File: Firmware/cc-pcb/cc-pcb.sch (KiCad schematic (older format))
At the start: 17 parts, among them CON1 BARREL_JACK, IC1 ATMEGA328P-A, P1 CONN_6, P2 CONN_6, P3 CONN_10, P4 CONN_6, P5 CONN_6, SW1 SRS

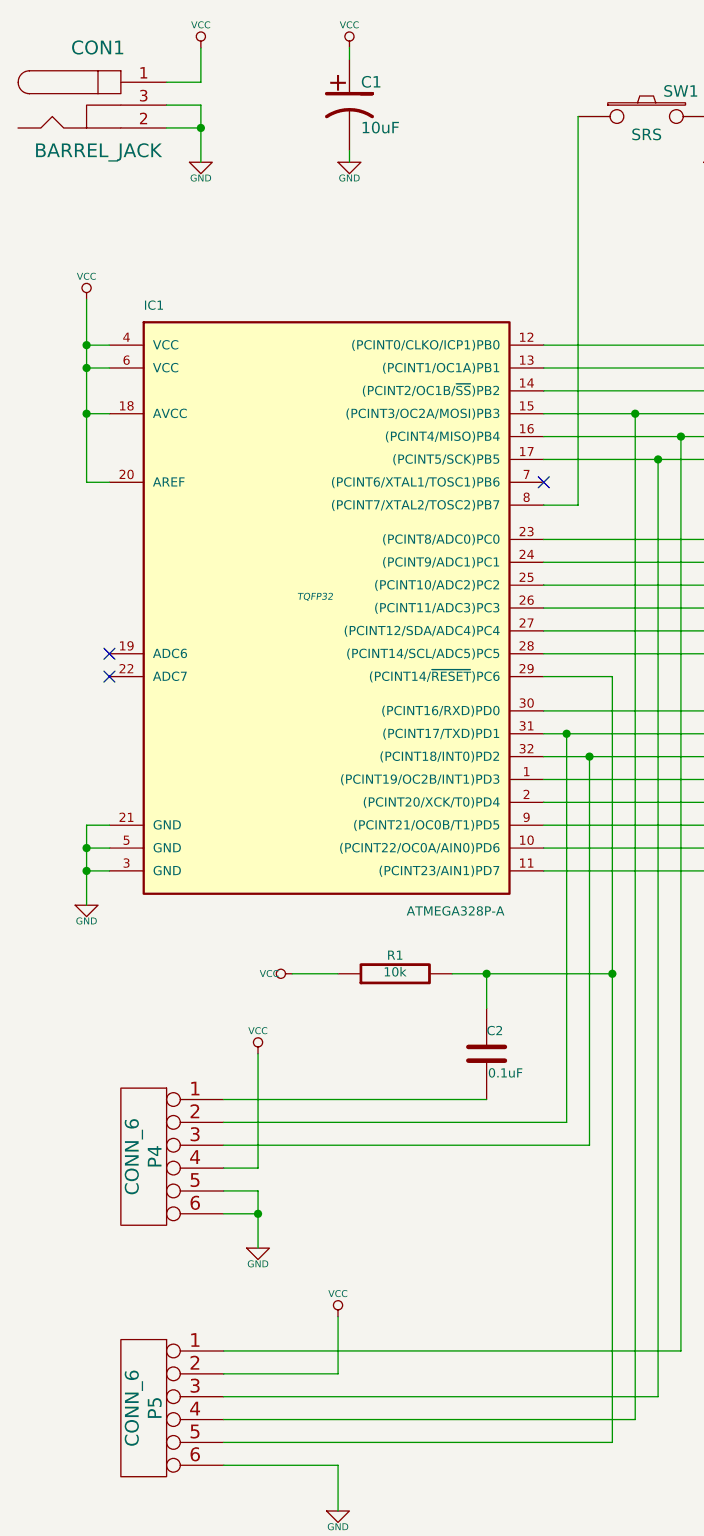
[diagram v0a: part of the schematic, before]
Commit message: Finishing schematics for PCB
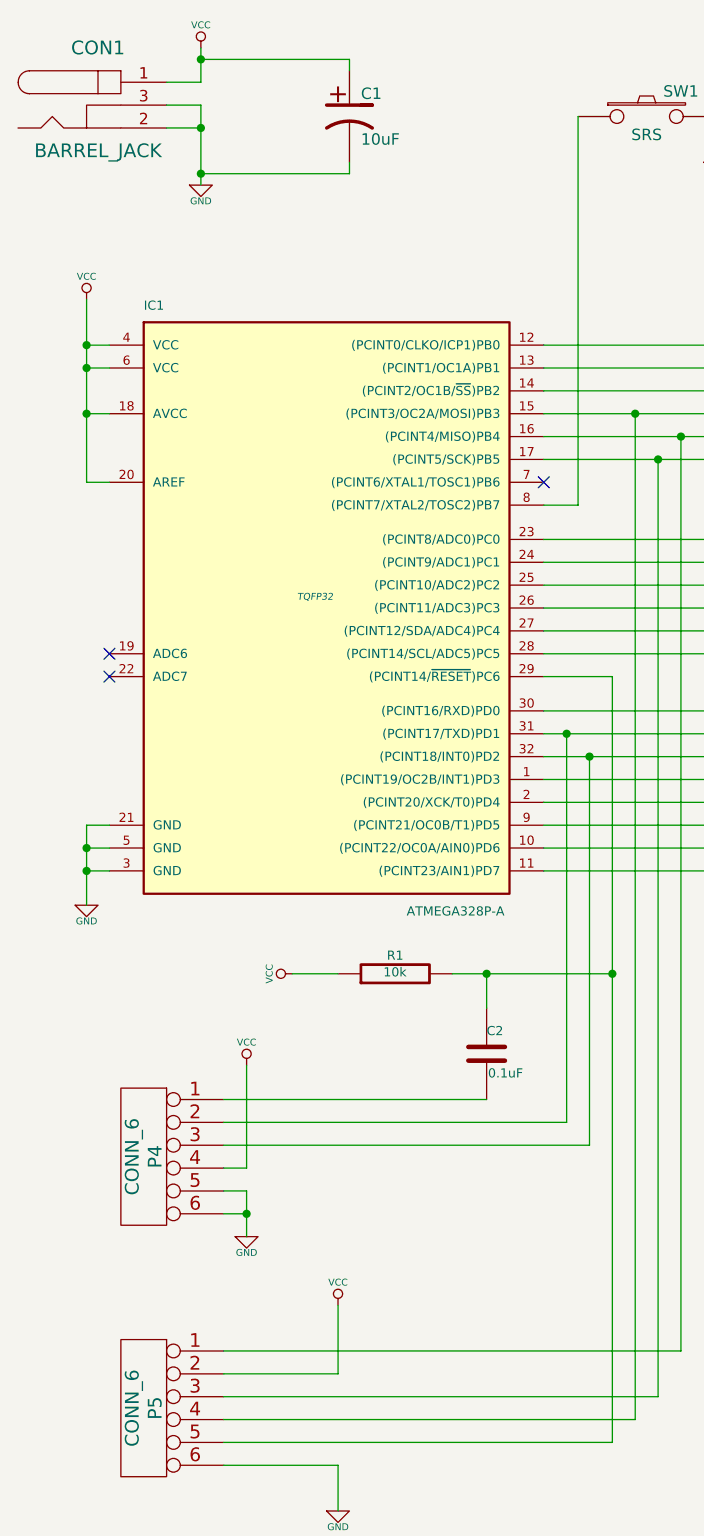
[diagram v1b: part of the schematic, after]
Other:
- moved on the sheet: C1

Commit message: Working on PCB
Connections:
- net VCC: no longer IC1.20 (AREF)
- no-connect marks 3 -> 4
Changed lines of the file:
@@
 Sheet 1 1
 Title "cc-schema.sch"
-Date "1 sep 2014"
+Date "2 sep 2014"
 Rev ""
 Comp ""
@@
 Wire Wire Line
 	2300 4100 2200 4100
-Connection ~ 2200 2100
-Wire Wire Line
-	2200 2100 2300 2100
-Connection ~ 2200 2000
-Wire Wire Line
-	2300 2000 2200 2000
 Wire Wire Line
 	5800 5300 6100 5300
@@
 Wire Wire Line
 	4800 6400 2800 6400
-Connection ~ 2200 2300
-Wire Wire Line
-	2200 2600 2300 2600
 Connection ~ 3950 4750
 Wire Wire Line
@@
 	2200 2300 2300 2300
 Wire Wire Line
-	2200 1800 2200 2600
-Wire Wire Line
-	2700 850  2700 700
-Wire Wire Line
-	2550 850  2700 850
+	2700 700  2700 850
+Wire Wire Line
+	2700 850  2550 850
 Connection ~ 2700 1050
 Wire Wire Line
@@
 	3350 1250 2700 1250
 Connection ~ 2700 1250
+$Comp
+L PWR_FLAG #FLG013
+U 1 1 5405B6E7
+P 2700 700
+F 0 "#FLG013" H 2700 795 30  0001 C CNN
+F 1 "PWR_FLAG" H 2700 880 30  0000 C CNN
+F 2 "" H 2700 700 60  0000 C CNN
+F 3 "" H 2700 700 60  0000 C CNN
+	1    2700 700
+	0    -1   -1   0
+$EndComp
+$Comp
+L PWR_FLAG #FLG014
+U 1 1 5405B6F6
+P 2700 1300
+F 0 "#FLG014" H 2700 1395 30  0001 C CNN
+F 1 "PWR_FLAG" H 2700 1480 30  0000 C CNN
+F 2 "" H 2700 1300 60  0000 C CNN
+F 3 "" H 2700 1300 60  0000 C CNN
+	1    2700 1300
+	0    -1   -1   0
+$EndComp
+NoConn ~ 2300 2600
+Wire Wire Line
+	2200 2300 2200 1800
+Wire Wire Line
+	2300 2100 2200 2100
+Connection ~ 2200 2100
+Wire Wire Line
+	2300 2000 2200 2000
+Connection ~ 2200 2000
 $EndSCHEMATC

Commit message: Finalyzing component list, fixing errors
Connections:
- net at IC1.30 ((PCINT16/RXD)PD0), P3.1 (P1): now also P4.3
- net at IC1.32 ((PCINT18/INT0)PD2), P3.3 (P3): no longer P4.3
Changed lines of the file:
@@
 Sheet 1 1
 Title "cc-schema.sch"
-Date "2 sep 2014"
+Date "4 sep 2014"
 Rev ""
 Comp ""
@@
 	2300 4200 2200 4200
 Wire Wire Line
-	2200 4100 2200 4450
+	2200 4100 2200 4200
+Wire Wire Line
+	2200 4200 2200 4300
+Wire Wire Line
+	2200 4300 2200 4450
 Wire Wire Line
 	2300 4100 2200 4100
@@
 Wire Wire Line
 	4200 3900 5500 3900
-Connection ~ 4400 3800
 Wire Wire Line
 	5600 3800 5600 4600
@@
 	5800 3600 5800 4400
 Wire Wire Line
-	4200 3600 5800 3600
+	4200 3600 4400 3600
+Wire Wire Line
+	4400 3600 5800 3600
 Connection ~ 4600 2300
 Connection ~ 4700 2500
@@
 	4500 3450 4200 3450
 Wire Wire Line
-	4500 3450 4500 6800
-Wire Wire Line
-	3800 4750 4500 4750
+	4500 3450 4500 4750
+Wire Wire Line
+	4500 4750 4500 6800
+Wire Wire Line
+	3800 4750 3950 4750
+Wire Wire Line
+	3950 4750 4500 4750
 Wire Wire Line
 	3100 4750 3300 4750
@@
 	2200 2300 2300 2300
 Wire Wire Line
-	2700 700  2700 850
+	2700 700  2700 750
+Wire Wire Line
+	2700 750  2700 850
 Wire Wire Line
 	2700 850  2550 850
@@
 	2550 1050 2700 1050
 Wire Wire Line
-	2700 950  2700 1300
+	2700 950  2700 1050
+Wire Wire Line
+	2700 1050 2700 1250
+Wire Wire Line
+	2700 1250 2700 1300
 Wire Wire Line
 	2550 950  2700 950
@@
 	4200 3800 5600 3800
 Wire Wire Line
-	4400 3800 4400 5500
+	4400 3600 4400 5500
 Wire Wire Line
 	4400 5500 2800 5500
 Wire Wire Line
-	4200 3700 5700 3700
+	4200 3700 4300 3700
+Wire Wire Line
+	4300 3700 5700 3700
 Wire Wire Line
 	4300 3700 4300 5400
@@
 	4350 2700 4350 1000
 Wire Wire Line
-	4200 2500 7600 2500
-Wire Wire Line
-	4200 2400 7200 2400
-Wire Wire Line
-	4200 2300 6800 2300
+	4200 2500 4700 2500
+Wire Wire Line
+	4700 2500 7600 2500
+Wire Wire Line
+	4200 2400 4800 2400
+Wire Wire Line
+	4800 2400 7200 2400
+Wire Wire Line
+	4200 2300 4600 2300
+Wire Wire Line
+	4600 2300 6800 2300
 Wire Wire Line
 	4200 2200 6400 2200
@@
 	2800 5700 2900 5700
 Wire Wire Line
-	2900 5700 2900 5900
+	2900 5700 2900 5800
+Wire Wire Line
+	2900 5800 2900 5900
 Wire Wire Line
 	2800 5800 2900 5800
@@
 NoConn ~ 2300 2600
 Wire Wire Line
-	2200 2300 2200 1800
+	2200 2300 2200 2100
+Wire Wire Line
+	2200 2100 2200 2000
+Wire Wire Line
+	2200 2000 2200 1800
 Wire Wire Line
 	2300 2100 2200 2100
@@
 	2300 2000 2200 2000
 Connection ~ 2200 2000
+Connection ~ 4400 3600
 $EndSCHEMATC

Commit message: Finalyzing component list, fixing errors
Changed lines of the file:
@@
 	2300 4200 2200 4200
 Wire Wire Line
-	2200 4100 2200 4200
-Wire Wire Line
-	2200 4200 2200 4300
-Wire Wire Line
-	2200 4300 2200 4450
+	2200 4100 2200 4450
 Wire Wire Line
 	2300 4100 2200 4100
@@
 	5800 3600 5800 4400
 Wire Wire Line
-	4200 3600 4400 3600
-Wire Wire Line
-	4400 3600 5800 3600
+	4200 3600 5800 3600
 Connection ~ 4600 2300
 Connection ~ 4700 2500
@@
 	4500 3450 4200 3450
 Wire Wire Line
-	4500 3450 4500 4750
-Wire Wire Line
-	4500 4750 4500 6800
-Wire Wire Line
-	3800 4750 3950 4750
-Wire Wire Line
-	3950 4750 4500 4750
+	4500 3450 4500 6800
+Wire Wire Line
+	3800 4750 4500 4750
 Wire Wire Line
 	3100 4750 3300 4750
@@
 	2200 2300 2300 2300
 Wire Wire Line
-	2700 700  2700 750
-Wire Wire Line
-	2700 750  2700 850
+	2700 700  2700 850
 Wire Wire Line
 	2700 850  2550 850
@@
 	2550 1050 2700 1050
 Wire Wire Line
-	2700 950  2700 1050
-Wire Wire Line
-	2700 1050 2700 1250
-Wire Wire Line
-	2700 1250 2700 1300
+	2700 950  2700 1300
 Wire Wire Line
 	2550 950  2700 950
@@
 	4400 5500 2800 5500
 Wire Wire Line
-	4200 3700 4300 3700
-Wire Wire Line
-	4300 3700 5700 3700
+	4200 3700 5700 3700
 Wire Wire Line
 	4300 3700 4300 5400
@@
 	4350 2700 4350 1000
 Wire Wire Line
-	4200 2500 4700 2500
-Wire Wire Line
-	4700 2500 7600 2500
-Wire Wire Line
-	4200 2400 4800 2400
-Wire Wire Line
-	4800 2400 7200 2400
-Wire Wire Line
-	4200 2300 4600 2300
-Wire Wire Line
-	4600 2300 6800 2300
+	4200 2500 7600 2500
+Wire Wire Line
+	4200 2400 7200 2400
+Wire Wire Line
+	4200 2300 6800 2300
 Wire Wire Line
 	4200 2200 6400 2200
@@
 	2800 5700 2900 5700
 Wire Wire Line
-	2900 5700 2900 5800
-Wire Wire Line
-	2900 5800 2900 5900
+	2900 5700 2900 5900
 Wire Wire Line
 	2800 5800 2900 5800
@@
 NoConn ~ 2300 2600
 Wire Wire Line
-	2200 2300 2200 2100
-Wire Wire Line
-	2200 2100 2200 2000
-Wire Wire Line
-	2200 2000 2200 1800
+	2200 1800 2200 2300
 Wire Wire Line
 	2300 2100 2200 2100

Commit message: Changed pcb to 2mm headers + neopixel power separated
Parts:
- removed P3: CONN_10, symbol CONN_10
- added P3: CONN_8, symbol CONN_8
- added P4: CONN_2, symbol CONN_2
- renumbered P4 to P5, P5 to P6
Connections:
- net GND: now also P4.2 (PM)
- net VCC: now also P4.1 (P1)
- net at IC1.1 ((PCINT19/OC2B/INT1)PD3): now also P3.4 (P4)
- net at IC1.10 ((PCINT22/OC0A/AIN0)PD6): now also P3.7 (P7)
- net at IC1.11 ((PCINT23/AIN1)PD7): now also P3.8 (P8)
- net at IC1.2 ((PCINT20/XCK/T0)PD4): now also P3.5 (P5)
- net at IC1.30 ((PCINT16/RXD)PD0), P5.3: now also P3.1 (P1)
- net at IC1.31 ((PCINT17/TXD)PD1), P5.2: now also P3.2 (P2)
- net at IC1.32 ((PCINT18/INT0)PD2): now also P3.3 (P3)
- net at IC1.9 ((PCINT21/OC0B/T1)PD5): now also P3.6 (P6)
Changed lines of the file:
@@
 Sheet 1 1
 Title "cc-schema.sch"
-Date "4 sep 2014"
+Date "11 sep 2014"
 Rev ""
 Comp ""
@@
 $EndComp
 $Comp
-L CONN_6 P4
+L CONN_6 P5
 U 1 1 53FA2625
 P 2450 5550
-F 0 "P4" V 2400 5550 60  0000 C CNN
+F 0 "P5" V 2400 5550 60  0000 C CNN
 F 1 "CONN_6" V 2500 5550 60  0000 C CNN
 F 2 "" H 2450 5550 60  0000 C CNN
@@
 $EndComp
 $Comp
-L CONN_6 P5
+L CONN_6 P6
 U 1 1 53FCECA3
 P 2450 6650
-F 0 "P5" V 2400 6650 60  0000 C CNN
+F 0 "P6" V 2400 6650 60  0000 C CNN
 F 1 "CONN_6" V 2500 6650 60  0000 C CNN
 F 2 "" H 2450 6650 60  0000 C CNN
@@
 	1    0    0    -1
 $EndComp
-$Comp
-L CONN_10 P3
-U 1 1 54048881
-P 6450 4850
-F 0 "P3" V 6400 4850 60  0000 C CNN
-F 1 "CONN_10" V 6500 4850 60  0000 C CNN
-F 2 "" H 6450 4850 60  0000 C CNN
-F 3 "" H 6450 4850 60  0000 C CNN
-	1    6450 4850
-	1    0    0    -1
-$EndComp
 NoConn ~ 4200 2600
 NoConn ~ 2300 3350
@@
 L VCC #PWR06
 U 1 1 54048FE9
-P 5500 5650
-F 0 "#PWR06" H 5500 5750 30  0001 C CNN
-F 1 "VCC" H 5500 5750 30  0000 C CNN
-F 2 "" H 5500 5650 60  0000 C CNN
-F 3 "" H 5500 5650 60  0000 C CNN
-	1    5500 5650
+P 5500 6000
+F 0 "#PWR06" H 5500 6100 30  0001 C CNN
+F 1 "VCC" H 5500 6100 30  0000 C CNN
+F 2 "" H 5500 6000 60  0000 C CNN
+F 3 "" H 5500 6000 60  0000 C CNN
+	1    5500 6000
 	-1   0    0    1
 $EndComp
@@
 L GND #PWR07
 U 1 1 54048FF8
-P 5800 5700
-F 0 "#PWR07" H 5800 5700 30  0001 C CNN
-F 1 "GND" H 5800 5630 30  0000 C CNN
-F 2 "" H 5800 5700 60  0000 C CNN
-F 3 "" H 5800 5700 60  0000 C CNN
-	1    5800 5700
+P 5800 6050
+F 0 "#PWR07" H 5800 6050 30  0001 C CNN
+F 1 "GND" H 5800 5980 30  0000 C CNN
+F 2 "" H 5800 6050 60  0000 C CNN
+F 3 "" H 5800 6050 60  0000 C CNN
+	1    5800 6050
 	1    0    0    -1
 $EndComp
@@
 	2300 4100 2200 4100
 Wire Wire Line
-	5800 5300 6100 5300
-Wire Wire Line
-	5800 5700 5800 5300
-Wire Wire Line
-	5500 5200 6100 5200
-Wire Wire Line
-	5500 5650 5500 5200
+	5800 5750 6100 5750
+Wire Wire Line
+	5800 6050 5800 5750
+Wire Wire Line
+	5500 5550 6100 5550
+Wire Wire Line
+	5500 6000 5500 5550
 Wire Wire Line
 	7600 1700 8200 1700
@@
 Connection ~ 2200 2000
 Connection ~ 4400 3600
+$Comp
+L CONN_8 P3
+U 1 1 5411ADE2
+P 6450 4750
+F 0 "P3" V 6400 4750 60  0000 C CNN
+F 1 "CONN_8" V 6500 4750 60  0000 C CNN
+F 2 "" H 6450 4750 60  0000 C CNN
+F 3 "" H 6450 4750 60  0000 C CNN
+	1    6450 4750
+	1    0    0    -1
+$EndComp
+$Comp
+L CONN_2 P4
+U 1 1 5411AEED
+P 6450 5650
+F 0 "P4" V 6400 5650 40  0000 C CNN
+F 1 "CONN_2" V 6500 5650 40  0000 C CNN
+F 2 "" H 6450 5650 60  0000 C CNN
+F 3 "" H 6450 5650 60  0000 C CNN
+	1    6450 5650
+	1    0    0    -1
+$EndComp
 $EndSCHEMATC
